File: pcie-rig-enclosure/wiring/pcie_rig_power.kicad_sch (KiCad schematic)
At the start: 13 parts, among them J1 XT60E-M 12V IN (REAR) - PSU l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, J2a 12V IN + red post (REAR, para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, J2b 12V IN - black post (REAR), J3 XT60E-F RISER (RIGHT), J4 XT60E-F CARD (RIGHT) - option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, J5a OUT + red post (RIGHT), J5b OUT - black post (RIGHT), J6 PROBE GND post (TOP) - scope 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, M1 Peacefair PZEM-031 1 LOAD- 2 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, SW1 Ampper rocker (TOP) A = from 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

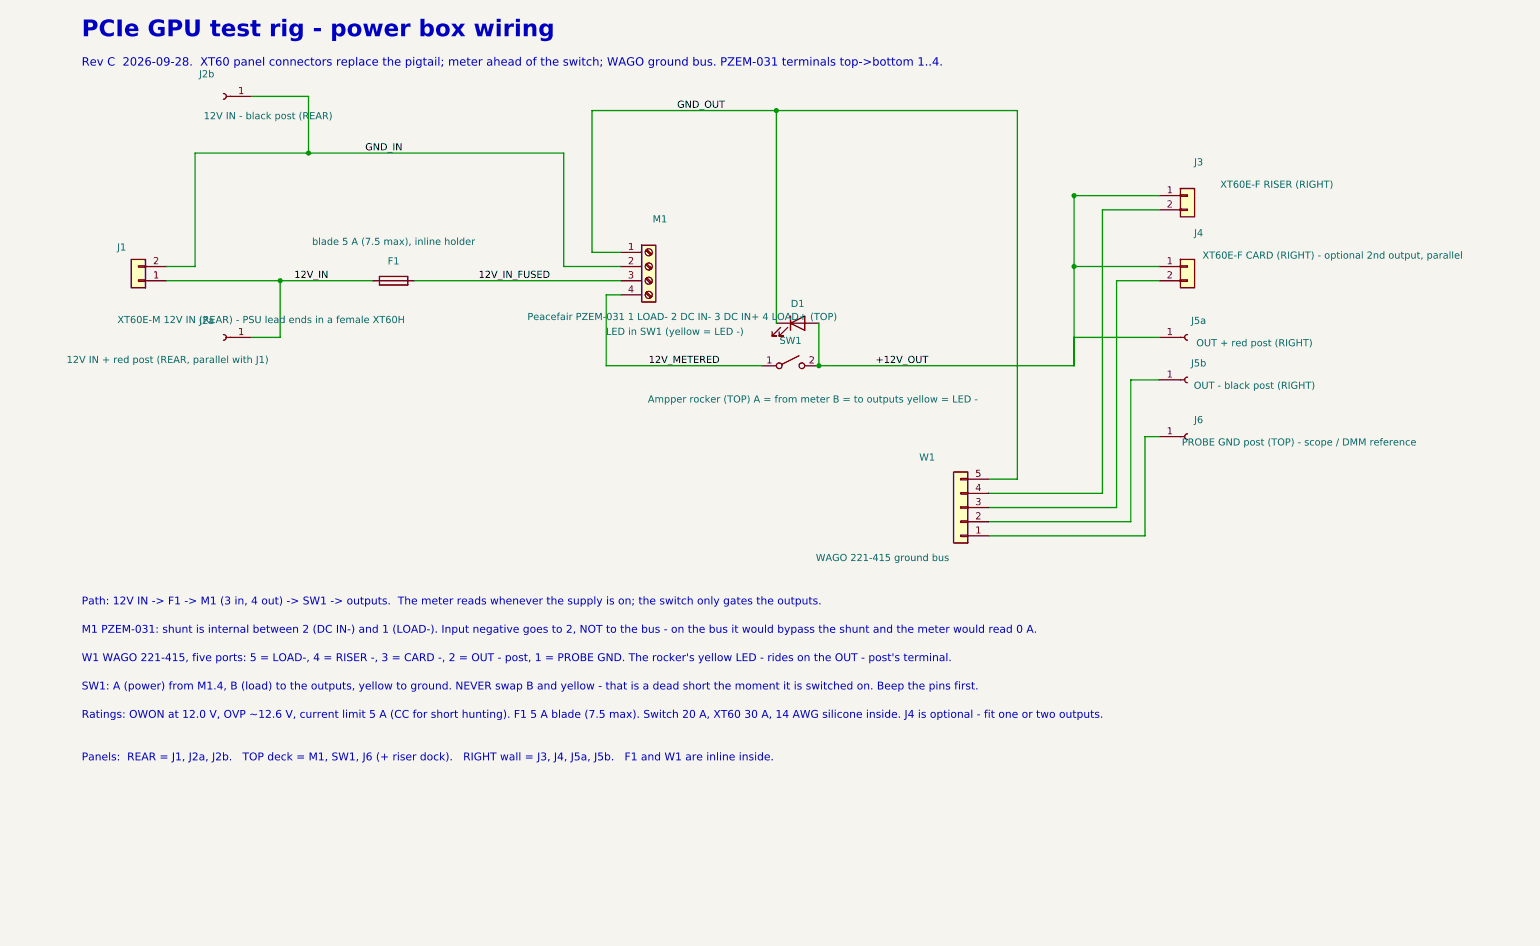
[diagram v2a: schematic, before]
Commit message: docs(pcie-rig-enclosure): schematic — short values on the sheet, parts legend table, notes trimmed
Signed-off-by: Aaron Cupp <mrcupp@mrcupp.com>
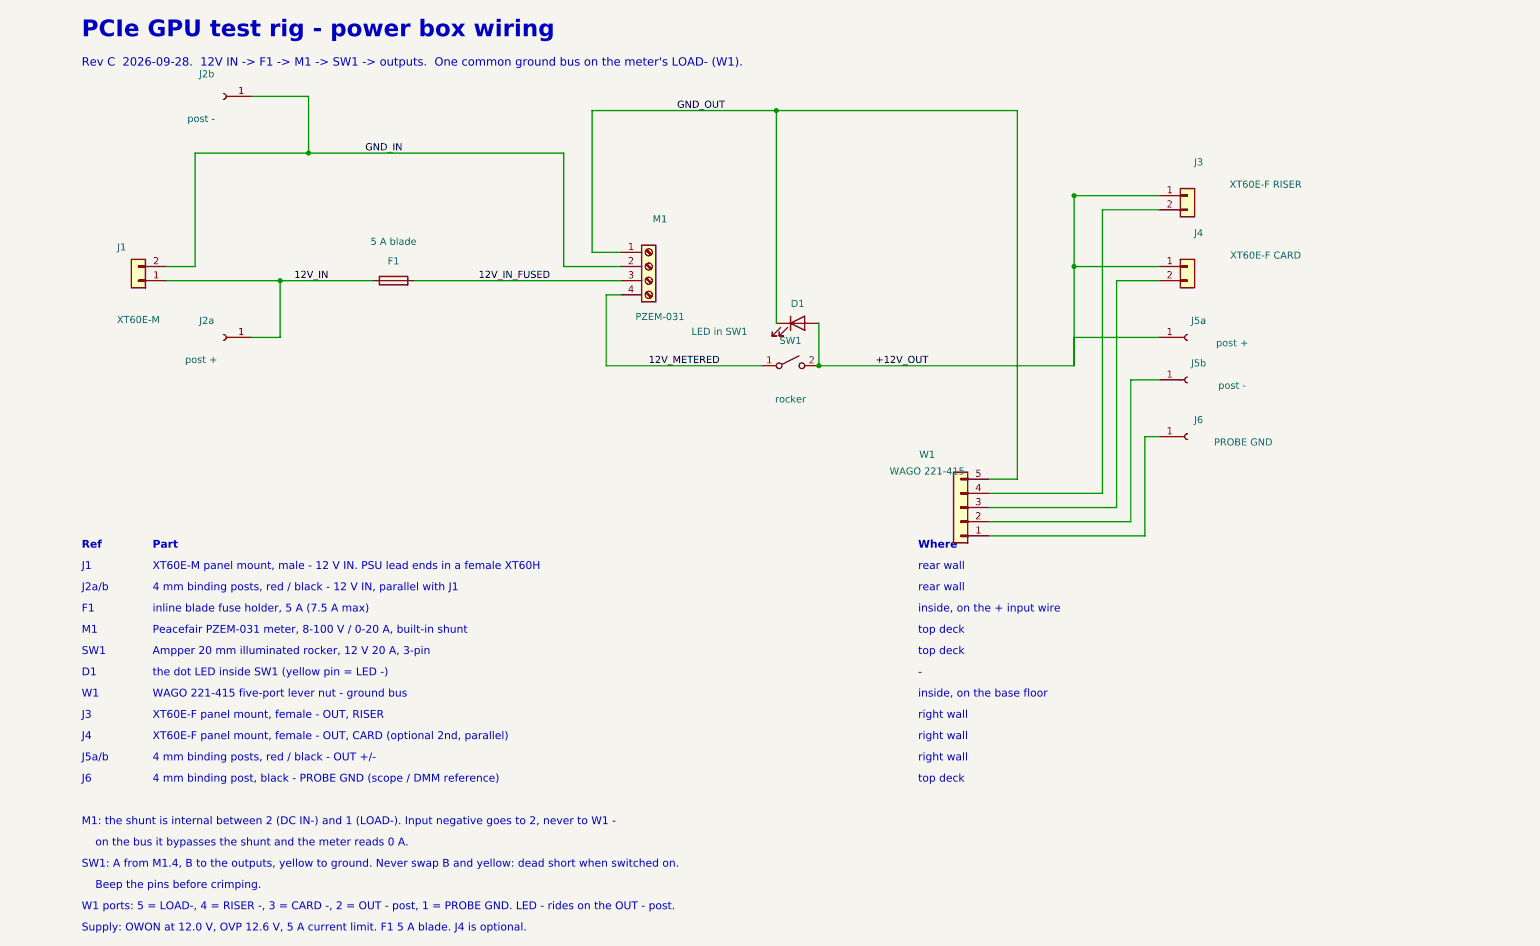
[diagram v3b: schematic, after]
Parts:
- D1: value LED in SW1 (yellow = LED -) -> LED in SW1
- F1: value blade 5 A (7.5 max), inline holder -> 5 A blade
- J1: value XT60E-M 12V IN (REAR) - PSU lead ends in a female XT60H -> XT60E-M
- J2a: value 12V IN + red post (REAR, parallel with J1) -> post +
- J2b: value 12V IN - black post (REAR) -> post -
- J3: value XT60E-F RISER (RIGHT) -> XT60E-F RISER
- J4: value XT60E-F CARD (RIGHT) - optional 2nd output, parallel -> XT60E-F CARD
- J5a: value OUT + red post (RIGHT) -> post +
- J5b: value OUT - black post (RIGHT) -> post -
- J6: value PROBE GND post (TOP) - scope / DMM reference -> PROBE GND
- M1: value Peacefair PZEM-031 1 LOAD- 2 DC IN- 3 DC IN+ 4 LOAD+ (TOP) -> PZEM-031
- SW1: value Ampper rocker (TOP) A = from meter B = to outputs yellow = LED - -> rocker
- W1: value WAGO 221-415 ground bus -> WAGO 221-415
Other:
- note added: "-"
- note added: "4 mm binding post, black - PROBE GND (scope / DMM reference)"
- note added: "4 mm binding posts, red / black - 12 V IN, parallel with J1"
- note added: "4 mm binding posts, red / black - OUT +/-"
- note added: "Ampper 20 mm illuminated rocker, 12 V 20 A, 3-pin"
- note added: "Beep the pins before crimping."
- note added: "D1"
- note added: "F1"
- note added: "J1"
- note added: "J2a/b"
- note added: "J3"
- note added: "J4"
- note added: "J5a/b"
- note added: "J6"
- note added: "M1"
- note added: "M1: the shunt is internal between 2 (DC IN-) and 1 (LOAD-). Input negative goes to 2, never to W1 -"
- note added: "Part"
- note added: "Peacefair PZEM-031 meter, 8-100 V / 0-20 A, built-in shunt"
- note added: "Ref"
- note added: "Rev C 2026-09-28. 12V IN -> F1 -> M1 -> SW1 -> outputs. One common ground bus on the meter's LOAD- (W1)."
- note added: "SW1"
- note added: "SW1: A from M1.4, B to the outputs, yellow to ground. Never swap B and yellow: dead short when switched on."
- note added: "Supply: OWON at 12.0 V, OVP 12.6 V, 5 A current limit. F1 5 A blade. J4 is optional."
- note added: "W1"
- note added: "W1 ports: 5 = LOAD-, 4 = RISER -, 3 = CARD -, 2 = OUT - post, 1 = PROBE GND. LED - rides on the OUT - post."
- note added: "WAGO 221-415 five-port lever nut - ground bus"
- note added: "Where"
- note added: "XT60E-F panel mount, female - OUT, CARD (optional 2nd, parallel)"
- note added: "XT60E-F panel mount, female - OUT, RISER"
- note added: "XT60E-M panel mount, male - 12 V IN. PSU lead ends in a female XT60H"
- note added: "inline blade fuse holder, 5 A (7.5 A max)"
- note added: "inside, on the + input wire"
- note added: "inside, on the base floor"
- note added: "on the bus it bypasses the shunt and the meter reads 0 A."
- note added: "rear wall"
- note added: "right wall"
- note added: "the dot LED inside SW1 (yellow pin = LED -)"
- note added: "top deck"
- note removed: "M1 PZEM-031: shunt is internal between 2 (DC IN-) and 1 (LOAD-). Input negative goes to 2, NOT to the bus - on the bus it would bypass the shunt and the meter would read 0 A."
- note removed: "Panels: REAR = J1, J2a, J2b. TOP deck = M1, SW1, J6 (+ riser dock). RIGHT wall = J3, J4, J5a, J5b. F1 and W1 are inline inside."
- note removed: "Path: 12V IN -> F1 -> M1 (3 in, 4 out) -> SW1 -> outputs. The meter reads whenever the supply is on; the switch only gates the outputs."
- note removed: "Ratings: OWON at 12.0 V, OVP ~12.6 V, current limit 5 A (CC for short hunting). F1 5 A blade (7.5 max). Switch 20 A, XT60 30 A, 14 AWG silicone inside. J4 is optional - fit one or two outputs."
- note removed: "Rev C 2026-09-28. XT60 panel connectors replace the pigtail; meter ahead of the switch; WAGO ground bus. PZEM-031 terminals top->bottom 1..4."
- note removed: "SW1: A (power) from M1.4, B (load) to the outputs, yellow to ground. NEVER swap B and yellow - that is a dead short the moment it is switched on. Beep the pins first."
- note removed: "W1 WAGO 221-415, five ports: 5 = LOAD-, 4 = RISER -, 3 = CARD -, 2 = OUT - post, 1 = PROBE GND. The rocker's yellow LED - rides on the OUT - post's terminal."

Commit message: feat(pcie-rig-enclosure): fit results — rocker 21.3, posts 7.6; 5x20 panel fuse back on the rear wall (8 A, 6 A limit); meter/fuse coupon with bed-face text
Signed-off-by: Aaron Cupp <mrcupp@mrcupp.com>
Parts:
- F1: value 5 A blade -> 5x20 8 A
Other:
- note added: "5x20 mm panel fuse holder, 8 A fast-blow glass fuse"
- note added: "Supply: OWON at 12.0 V, OVP 12.6 V, 6 A current limit (the working max). F1 8 A fast 5x20. J4 is optional."
- note removed: "Supply: OWON at 12.0 V, OVP 12.6 V, 5 A current limit. F1 5 A blade. J4 is optional."
- note removed: "inline blade fuse holder, 5 A (7.5 A max)"
- note removed: "inside, on the + input wire"
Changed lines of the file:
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@@
 	)
 	(text
-		"inline blade fuse holder, 5 A (7.5 A max)"
+		"5x20 mm panel fuse holder, 8 A fast-blow glass fuse"
 		(exclude_from_sim no)
 		(at 33.019999999999996 125.72999999999999 0)
@@
 	)
 	(text
-		"inside, on the + input wire"
+		"rear wall"
 		(exclude_from_sim no)
 		(at 170.18 125.72999999999999 0)
@@
 	)
 	(text
-		"Supply: OWON at 12.0 V, OVP 12.6 V, 5 A current limit. F1 5 A blade. J4 is optional."
+		"Supply: OWON at 12.0 V, OVP 12.6 V, 6 A current limit (the working max). F1 8 A fast 5x20. J4 is optional."
 		(exclude_from_sim no)
 		(at 20.32 182.88 0)
@@
 		(dnp no)
 		(property "Reference" "F1" (at 76.2 62.54 270) (effects (font (size 1.27 1.27))))
-		(property "Value" "5 A blade" (at 76.2 59.04 270) (effects (font (size 1.27 1.27))))
+		(property "Value" "5x20  8 A" (at 76.2 59.04 270) (effects (font (size 1.27 1.27))))
 		(property "Footprint" "" (at 76.2 66.04 0) (effects (font (size 1.27 1.27)) (hide yes)))
 		(property "Datasheet" "" (at 76.2 66.04 0) (effects (font (size 1.27 1.27)) (hide yes)))
